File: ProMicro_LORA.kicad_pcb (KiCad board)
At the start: 2 copper layers, 17.8 x 30.5 mm, 44 parts, among them J1 SMA, J2 COAX, U1 SX1276, U2 AS179-92LF, Y1 32Mhz

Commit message: new docu
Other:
- board text added: "github.com/nerdyscout/ProMicro_LORA"
- board text removed: "github.com/nerdyscout/ProMicro_SX1276"

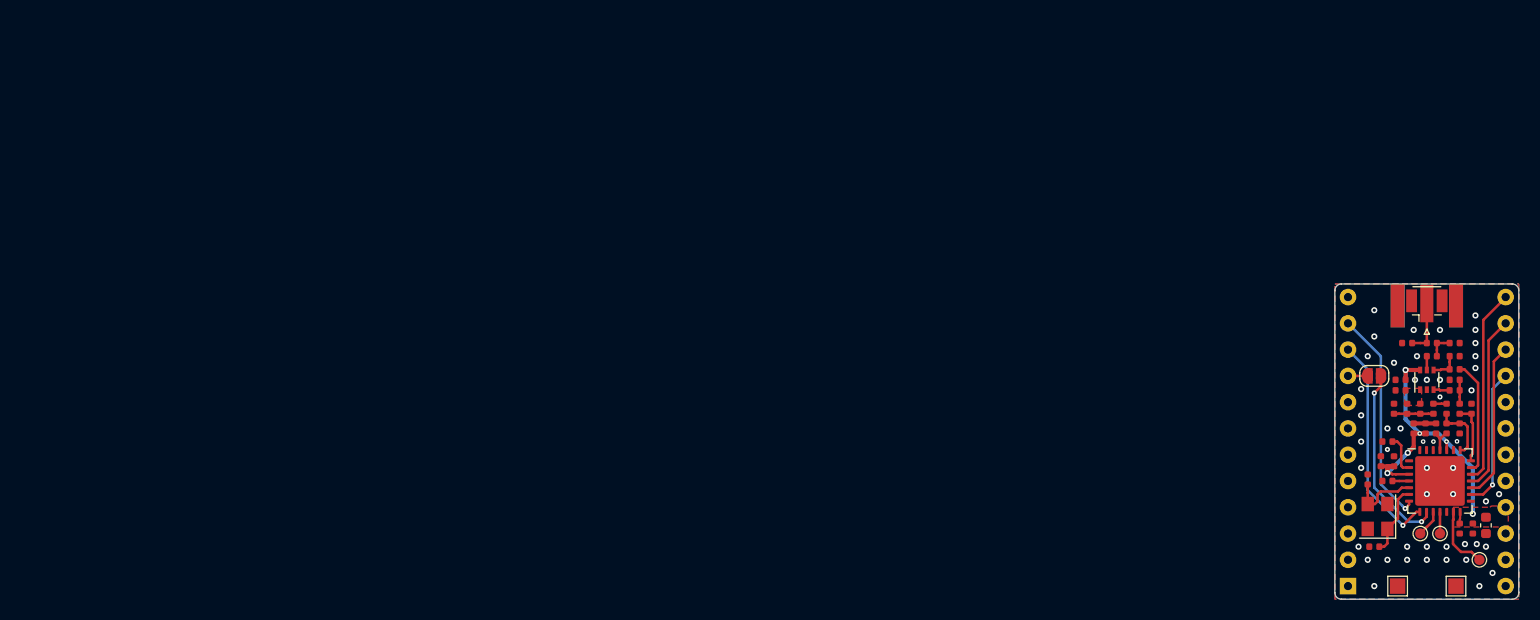
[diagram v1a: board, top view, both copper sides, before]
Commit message: pin docu and wider holes
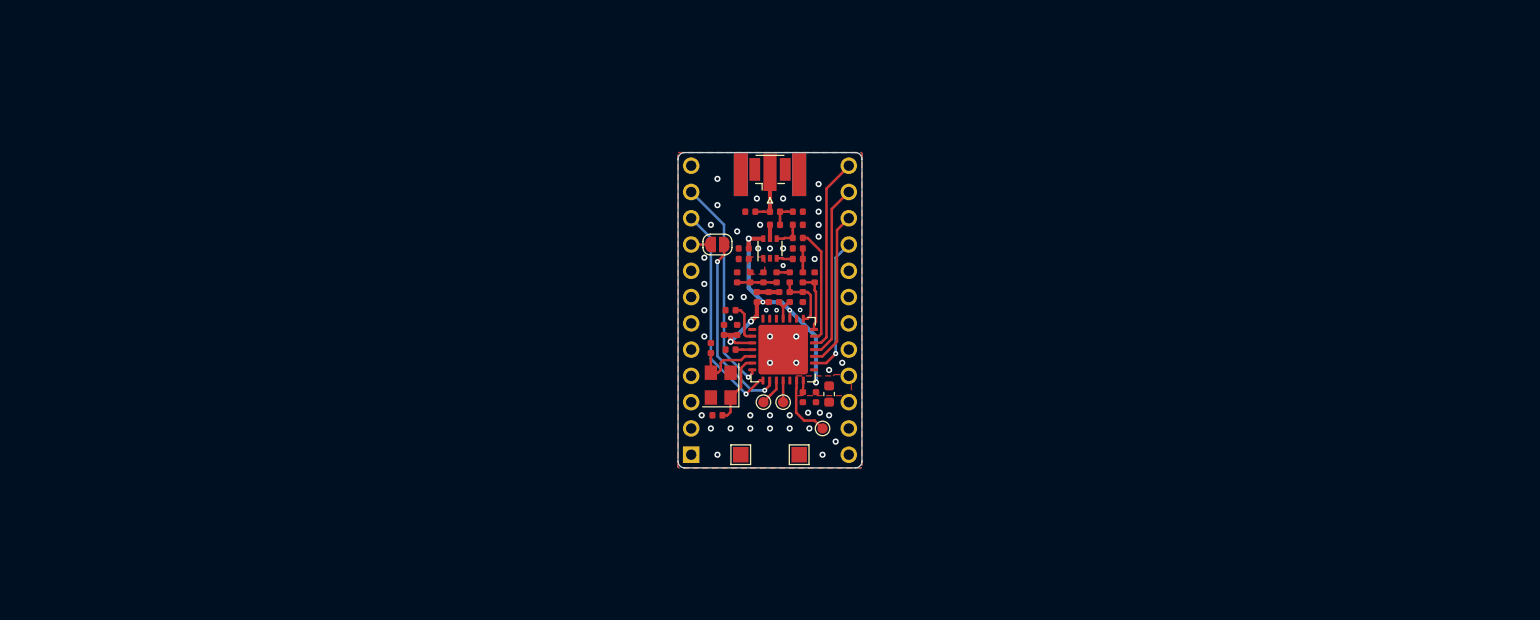
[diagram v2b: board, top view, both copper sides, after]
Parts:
- moved A1 64.8 mm to (127.0, 104.1)
- moved C1 64.8 mm to (129.5, 100.3)
- moved C10 64.8 mm to (137.3, 80.6)
- moved C11 64.8 mm to (132.7, 80.6)
- moved C12 64.8 mm to (132.7, 87.0)
- moved C13 64.8 mm to (137.3, 81.9)
- moved C14 64.8 mm to (132.1, 84.2)
- moved C15 64.8 mm to (134.5, 88.9)
- moved C16 64.8 mm to (133.3, 88.9)
- moved C17 64.8 mm to (137.8, 98.6)
- moved C18 64.8 mm to (130.2, 92.1)
- moved C19 64.8 mm to (131.4, 92.1)
- moved C2 64.8 mm to (137.8, 88.9)
- moved C20 64.8 mm to (130.8, 94.0)
- moved C21 64.8 mm to (130.8, 90.2)
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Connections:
- A1 pad 3: GND -> (no net)
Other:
- board text added: "3V"
- board text added: "CS"
- board text added: "DIO0"
- board text added: "DIO1"
- board text added: "GND"
- board text added: "MISO"
- board text added: "MOSI"
- board text added: "SCK"
- board text added: "v1.1"
- board text added: "~RESET"
- board text removed: "v1.0"

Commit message: upgrade
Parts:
- LOGO1: footprint Symbol:OSHW-Logo2_9.8x8mm_SilkScreen -> Symbol:OSHW-Symbol_6.7x6mm_SilkScreen
- TP2: value TestPoint -> DIO2
- TP3: value TestPoint -> DIO3
- TP4: value TestPoint -> DIO5
- moved C18 64.8 mm to (66.7, 79.4)
- moved C8 64.8 mm to (68.6, 72.5)
- moved L4 64.8 mm to (70.5, 74.3)
- moved TP2 64.8 mm to (70.5, 86.4)
- moved A1 64.8 mm to (63.5, 91.4)
- moved C10 64.8 mm to (73.8, 67.9)
- moved C11 64.8 mm to (69.2, 67.9)
- moved C12 64.8 mm to (69.2, 74.3)
- moved C13 64.8 mm to (73.8, 69.2)
- moved C14 64.8 mm to (68.6, 71.5)
- moved C15 64.8 mm to (71.0, 76.2)
- moved C16 64.8 mm to (69.8, 76.2)
- moved C19 64.8 mm to (67.9, 79.4)
- moved C20 64.8 mm to (67.3, 81.3)
- moved C21 64.8 mm to (67.3, 77.5)
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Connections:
- A1 pad 8: (no net) -> D5
- A1 pad 9: D6 -> (no net)
- JP1 pad 2: D6 -> D5
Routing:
- net Net-(JP1-Pad1): track 18.2 -> 13.4 mm
- net D5: track 0.00 -> 2.80 mm
- net D6: track 1.89 -> 0.00 mm
- net GND: vias 49 -> 51
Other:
- board text added: "github.com/nerdyscout/ProMicro/LORA"
- board text removed: "github.com/nerdyscout/ProMicro_LORA"

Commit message: kicad-exports
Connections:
- net MISO renamed D14
- net MOSI renamed D16
- net SCK renamed D15
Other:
- board text added: "CIPO"
- board text added: "CLK"
- board text added: "COPI"
- board text removed: "MISO"
- board text removed: "MOSI"
- board text removed: "SCK"
